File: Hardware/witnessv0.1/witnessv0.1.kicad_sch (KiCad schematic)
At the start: 0 parts

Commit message: power updates and some esp32 stuff
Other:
- added sheet Radio (radio.kicad_sch)
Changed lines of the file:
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@@
 	)
 	(sheet
-		(at 172.72 66.04)
+		(at 111.76 36.83)
+		(size 46.99 46.99)
+		(exclude_from_sim no)
+		(in_bom yes)
+		(on_board yes)
+		(dnp no)
+		(fields_autoplaced yes)
+		(stroke
+			(width 0.1524)
+			(type solid)
+		)
+		(fill
+			(color 0 0 0 0)
+		)
+		(property "Sheetname" "Radio"
+			(at 111.76 36.1184 0)
+			(show_name no)
+			(do_not_autoplace no)
+			(effects
+				(font
+					(size 1.27 1.27)
+				)
+				(justify left bottom)
+			)
+		)
+		(property "Sheetfile" "radio.kicad_sch"
+			(at 111.76 84.4046 0)
+			(show_name no)
+			(do_not_autoplace no)
+			(effects
+				(font
+					(size 1.27 1.27)
+				)
+				(justify left top)
+			)
+		)
+		(instances
+			(project "witnessv0.1"
+				(path "/c7e4a338-55e7-4896-822a-22161197db9b"
+					(page "6")
+				)
+			)
+		)
+	)
+	(sheet
+		(at 199.39 31.75)
 		(size 58.42 39.37)
 		(exclude_from_sim no)
@@
 		)
 		(property "Sheetname" "Power"
-			(at 172.72 65.3284 0)
+			(at 199.39 31.0384 0)
 			(show_name no)
 			(do_not_autoplace no)
@@
 		)
 		(property "Sheetfile" "power.kicad_sch"
-			(at 172.72 105.9946 0)
+			(at 199.39 71.7046 0)
 			(show_name no)
 			(do_not_autoplace no)

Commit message: lots of work
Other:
- sheet IO ports: added USB_D+, USB_D-; removed none
- sheet Radio ports: added RAD_BUSY, RAD_CS, RAD_DIO1, RAD_RF_EN, RAD_RST, SPI1_CIPO, SPI1_COPI, SPI1_SCLK; removed none
- company: (none) -> WITNESS

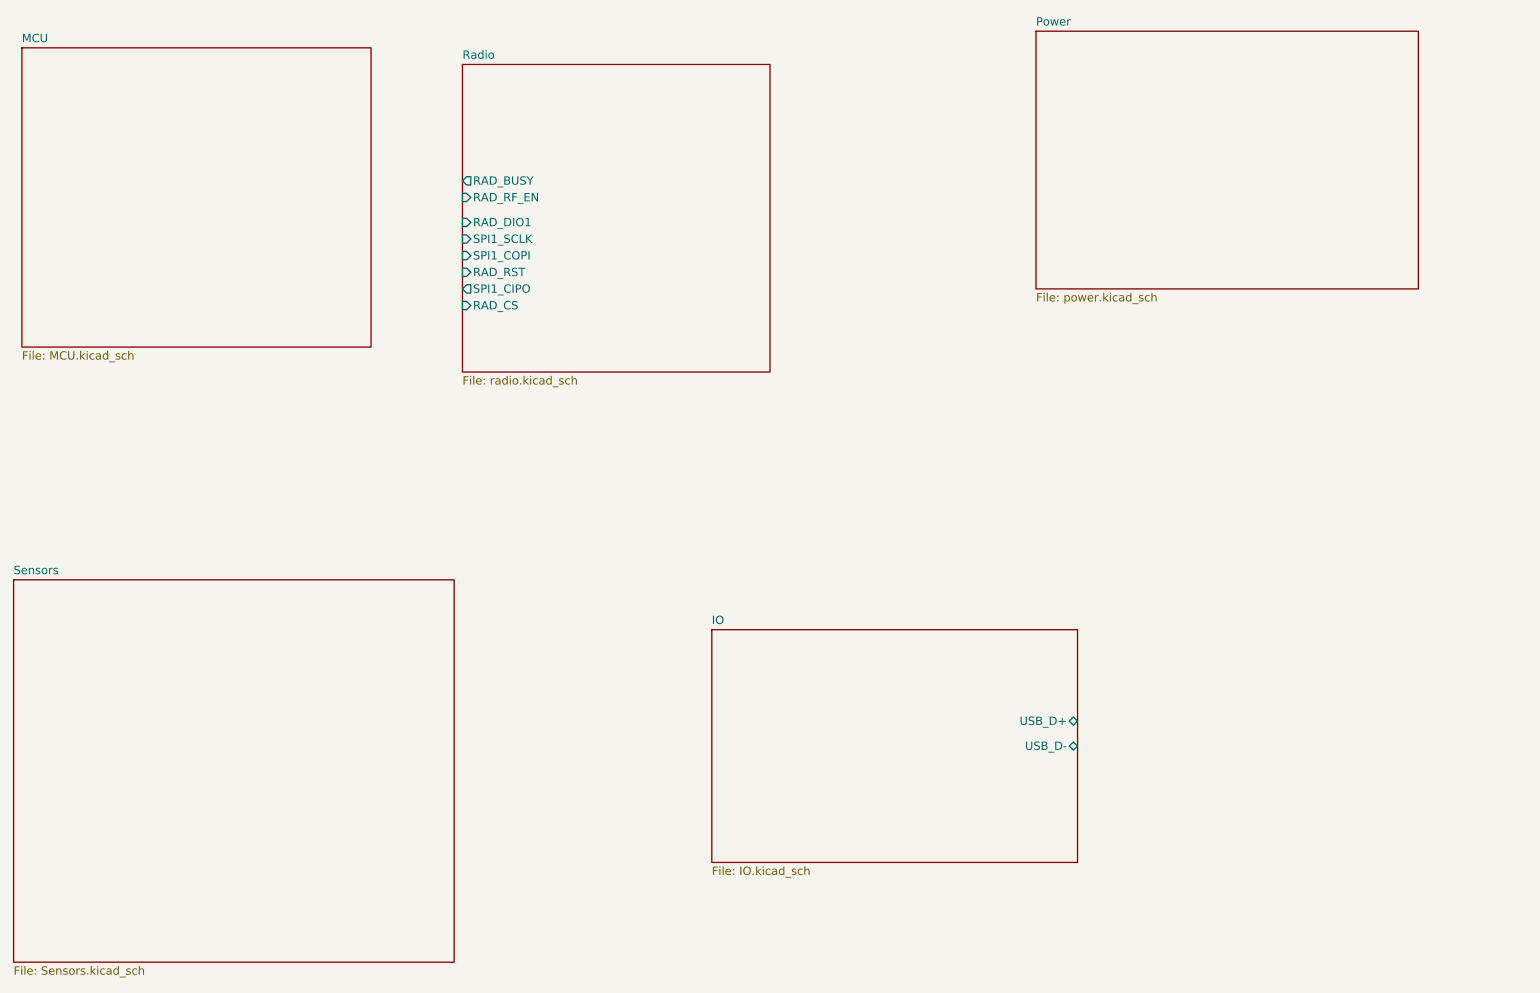
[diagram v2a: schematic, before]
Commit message: micro lock conenctors and sd card soldered to baord and inital palcement done.
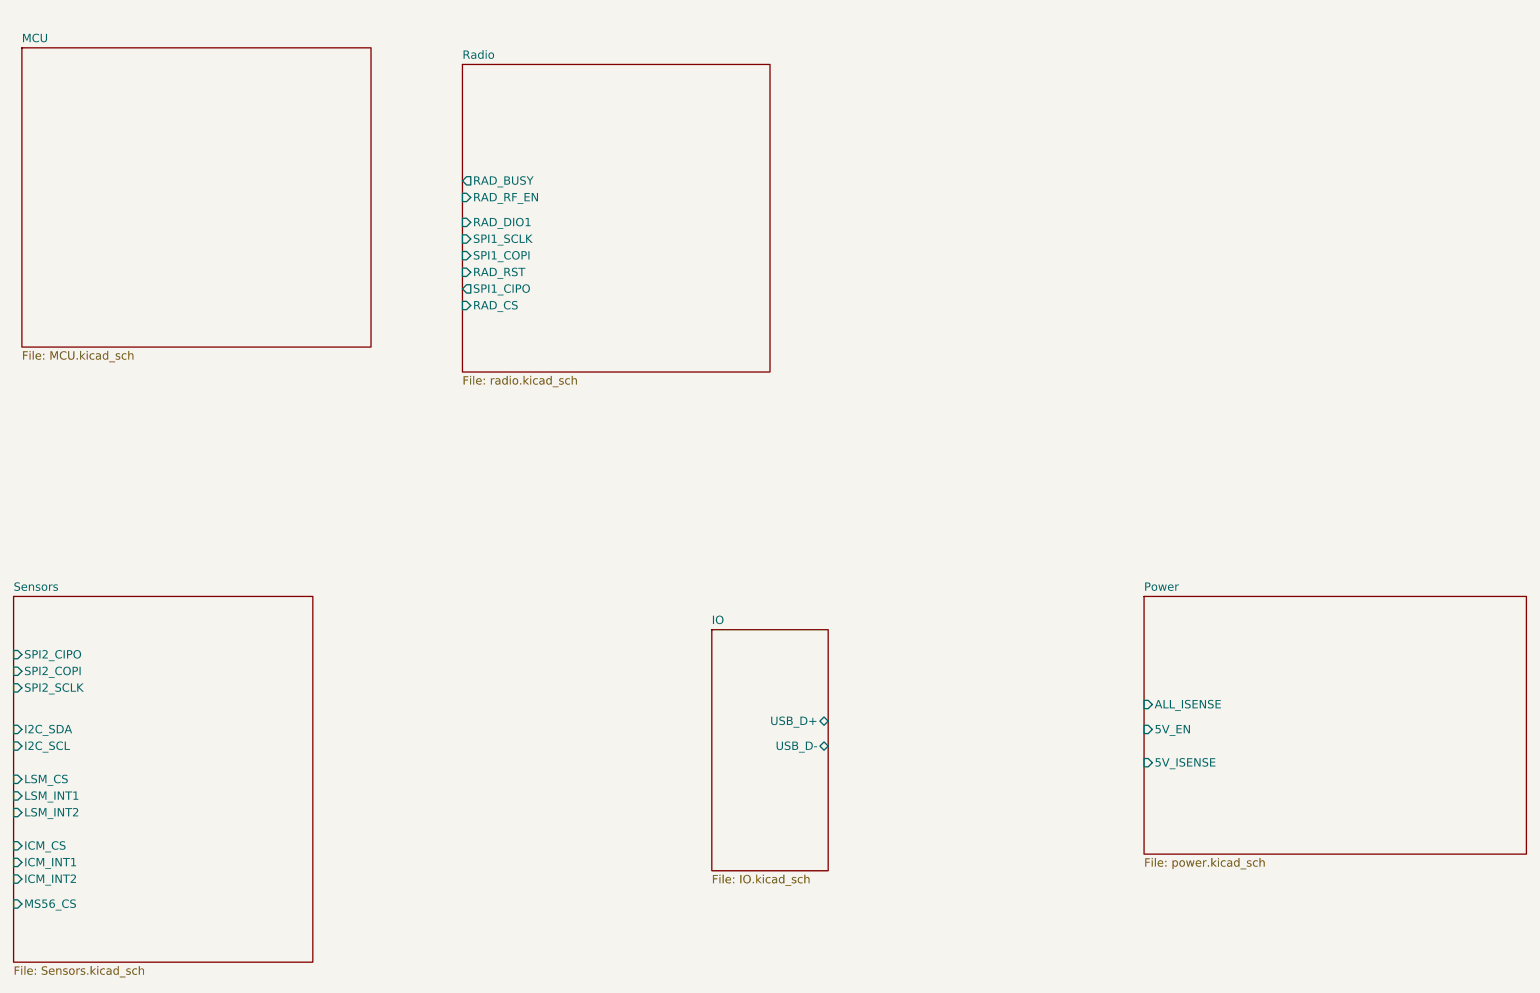
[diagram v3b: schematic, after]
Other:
- sheet Power ports: added 5V_EN, 5V_ISENSE, ALL_ISENSE; removed none
- sheet Sensors ports: added I2C_SCL, I2C_SDA, ICM_CS, ICM_INT1, ICM_INT2, LSM_CS, LSM_INT1, LSM_INT2, MS56_CS, SPI2_CIPO, SPI2_COPI, SPI2_SCLK; removed none
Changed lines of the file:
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@@
 	(sheet
 		(at 149.86 123.19)
-		(size 55.88 35.56)
+		(size 17.78 36.83)
 		(exclude_from_sim no)
 		(in_bom yes)
@@
 		)
 		(property "Sheetfile" "IO.kicad_sch"
-			(at 149.86 159.3346 0)
+			(at 149.86 160.6046 0)
 			(show_name no)
 			(do_not_autoplace no)
@@
 		)
 		(pin "USB_D+" bidirectional
-			(at 205.74 137.16 0)
+			(at 167.64 137.16 0)
 			(effects
 				(font
@@
 		)
 		(pin "USB_D-" bidirectional
-			(at 205.74 140.97 0)
+			(at 167.64 140.97 0)
 			(effects
 				(font
@@
 	)
 	(sheet
-		(at 43.18 115.57)
-		(size 67.31 58.42)
+		(at 43.18 118.11)
+		(size 45.72 55.88)
 		(exclude_from_sim no)
 		(in_bom yes)
@@
 		)
 		(property "Sheetname" "Sensors"
-			(at 43.18 114.8584 0)
+			(at 43.18 117.3984 0)
 			(show_name no)
 			(do_not_autoplace no)
@@
 				)
 				(justify left top)
+			)
+		)
+		(pin "LSM_INT1" input
+			(at 43.18 148.59 180)
+			(effects
+				(font
+					(size 1.27 1.27)
+				)
+				(justify left)
+			)
+		)
+		(pin "LSM_INT2" input
+			(at 43.18 151.13 180)
+			(effects
+				(font
+					(size 1.27 1.27)
+				)
+				(justify left)
+			)
+		)
+		(pin "I2C_SDA" input
+			(at 43.18 138.43 180)
+			(effects
+				(font
+					(size 1.27 1.27)
+				)
+				(justify left)
+			)
+		)
+		(pin "ICM_INT2" input
+			(at 43.18 161.29 180)
+			(effects
+				(font
+					(size 1.27 1.27)
+				)
+				(justify left)
+			)
+		)
+		(pin "SPI2_COPI" input
+			(at 43.18 129.54 180)
+			(effects
+				(font
+					(size 1.27 1.27)
+				)
+				(justify left)
+			)
+		)
+		(pin "SPI2_CIPO" input
+			(at 43.18 127 180)
+			(effects
+				(font
+					(size 1.27 1.27)
+				)
+				(justify left)
+			)
+		)
+		(pin "MS56_CS" input
+			(at 43.18 165.1 180)
+			(effects
+				(font
+					(size 1.27 1.27)
+				)
+				(justify left)
+			)
+		)
+		(pin "LSM_CS" input
+			(at 43.18 146.05 180)
+			(effects
+				(font
+					(size 1.27 1.27)
+				)
+				(justify left)
+			)
+		)
+		(pin "SPI2_SCLK" input
+			(at 43.18 132.08 180)
+			(effects
+				(font
+					(size 1.27 1.27)
+				)
+				(justify left)
+			)
+		)
+		(pin "ICM_INT1" input
+			(at 43.18 158.75 180)
+			(effects
+				(font
+					(size 1.27 1.27)
+				)
+				(justify left)
+			)
+		)
+		(pin "ICM_CS" input
+			(at 43.18 156.21 180)
+			(effects
+				(font
+					(size 1.27 1.27)
+				)
+				(justify left)
+			)
+		)
+		(pin "I2C_SCL" input
+			(at 43.18 140.97 180)
+			(effects
+				(font
+					(size 1.27 1.27)
+				)
+				(justify left)
 			)
 		)
@@
 	)
 	(sheet
-		(at 199.39 31.75)
+		(at 215.9 118.11)
 		(size 58.42 39.37)
 		(exclude_from_sim no)
@@
 		)
 		(property "Sheetname" "Power"
-			(at 199.39 31.0384 0)
+			(at 215.9 117.3984 0)
 			(show_name no)
 			(do_not_autoplace no)
@@
 		)
 		(property "Sheetfile" "power.kicad_sch"
-			(at 199.39 71.7046 0)
+			(at 215.9 158.0646 0)
 			(show_name no)
 			(do_not_autoplace no)
@@
 			)
 		)
+		(pin "ALL_ISENSE" input
+			(at 215.9 134.62 180)
+			(effects
+				(font
+					(size 1.27 1.27)
+				)
+				(justify left)
+			)
+		)
+		(pin "5V_EN" input
+			(at 215.9 138.43 180)
+			(effects
+				(font
+					(size 1.27 1.27)
+				)
+				(justify left)
+			)
+		)
+		(pin "5V_ISENSE" input
+			(at 215.9 143.51 180)
+			(effects
+				(font
+					(size 1.27 1.27)
+				)
+				(justify left)
+			)
+		)
